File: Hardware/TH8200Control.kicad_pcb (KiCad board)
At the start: 2 copper layers, 113 x 49 mm, 41 parts, among them J1 Mains, J2 Heater Relay, J3 Motor, Q1 BC817, Q2 SFH 300, Q3 BC817, Q4 BC817, T1 BV EI 306 3601, U1 CNY17-3, U2 CNY17-3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

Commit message: Add OSHW logo and GitHub link to PCB
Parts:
- added REF***: OSHW-Symbol_6.7x6mm_SilkScreen, Symbols:OSHW-Symbol_6.7x6mm_SilkScreen, B.Cu at (89.0, 54.5)
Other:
- board text added: "github.com/Mezgrman/TH8200Control"

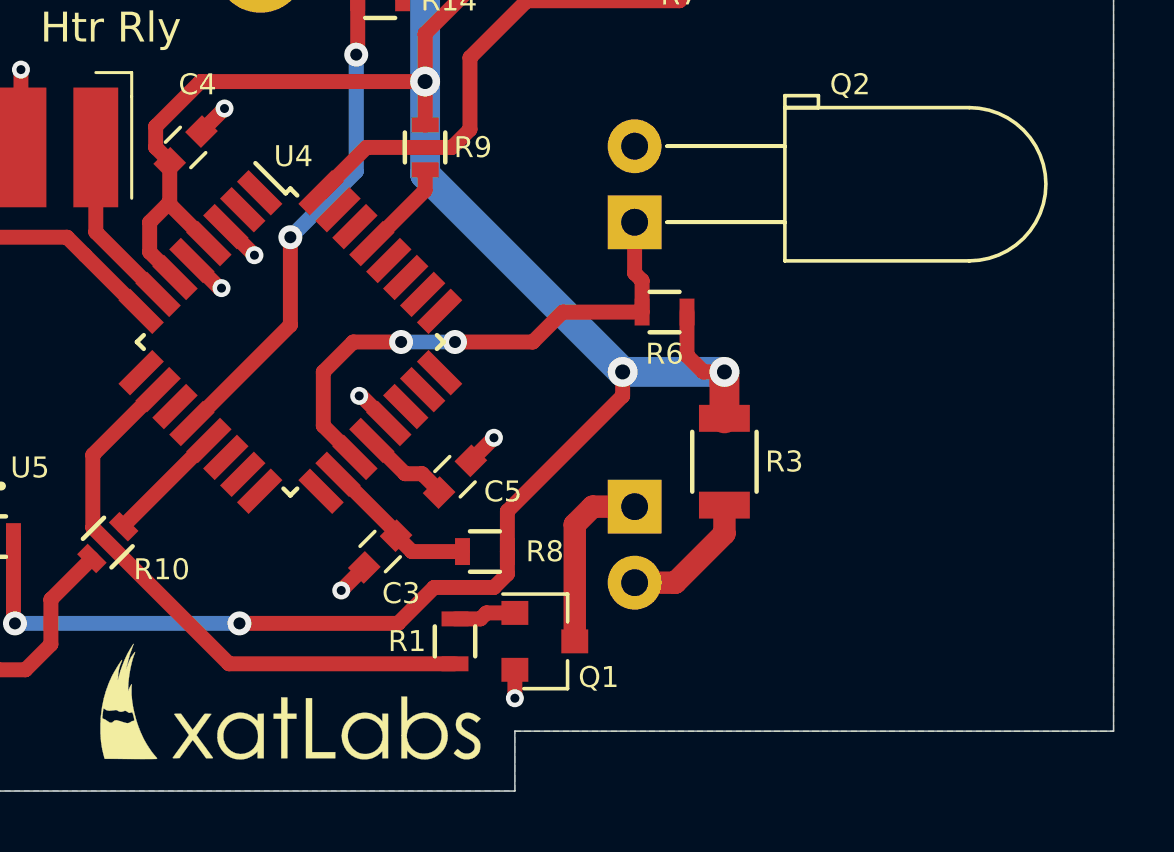
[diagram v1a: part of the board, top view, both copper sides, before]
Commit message: Add ISP header
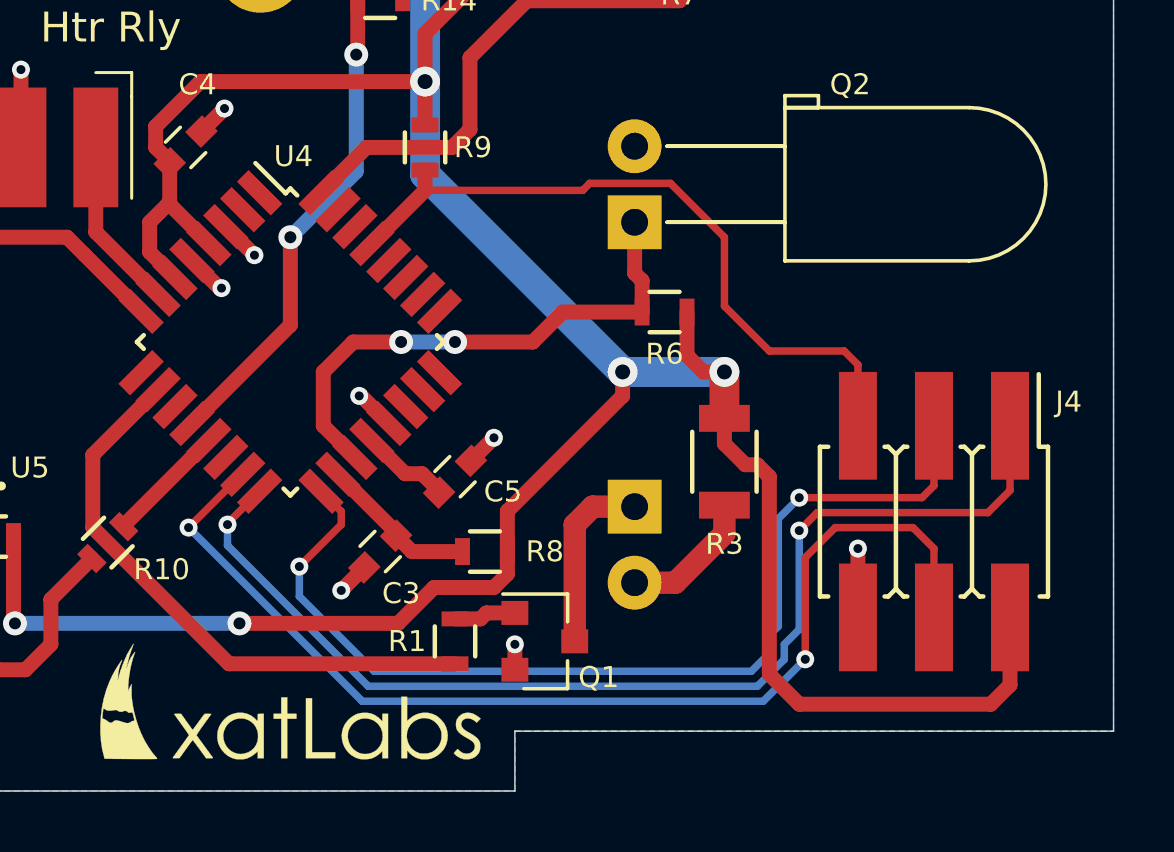
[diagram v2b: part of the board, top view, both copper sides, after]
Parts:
- added J4: ISP, Pin_Headers:Pin_Header_Straight_SMT_02x03, F.Cu at (161.0, 88.0)
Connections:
- net Net-(R9-Pad1) renamed ISP_RESET
- U4 pad 15: Net-(U4-Pad15) -> ISP_COPI
- U4 pad 16: Net-(U4-Pad16) -> ISP_CIPO
- U4 pad 17: Net-(U4-Pad17) -> ISP_SCK
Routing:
- net ISP_CIPO: track 0.00 -> 37.4 mm, vias 0 -> 2
- net ISP_COPI: track 0.00 -> 36.8 mm, vias 0 -> 2
- net ISP_SCK: track 0.00 -> 33.6 mm, vias 0 -> 2
- net ISP_RESET: track 3.20 -> 23.7 mm
- net +5V: track 95.3 -> 115.7 mm
- net GND: track 31.1 -> 33.3 mm, vias 29 -> 30
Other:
- board text added: "Control board for Siemens TH8200 hand dryer v1.0 / 22.07.2020 Julian Metzler xatlabs.com"
- board text removed: "Control board for Siemens TH8200 hand dryer v1.0 / 20.07.2020 Julian Metzler xatlabs.com"

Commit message: Fix polarity of C1
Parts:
- turned C1 to 90 degrees
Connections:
- C1 pad 1: GND -> +12V
- C1 pad 2: +12V -> GND
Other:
- board text added: "Control board for Siemens TH8200 hand dryer v1.1 / 29.07.2020 Julian Metzler xatlabs.com"
- board text removed: "Control board for Siemens TH8200 hand dryer v1.0 / 22.07.2020 Julian Metzler xatlabs.com"
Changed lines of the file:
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@@
   (title_block
     (title "Control board for Siemens TH8200 hand dryer")
-    (date 2020-07-22)
-    (rev 1.0)
+    (date 2020-07-29)
+    (rev 1.1)
     (company xatLabs)
     (comment 1 "Julian Metzler")
@@
   )
   (module Capacitors_SMD:CP_Elec_6.3x7.7 (layer F.Cu)
-    (at 121 54.5 270)
+    (at 121 54.5 90)
     (descr "SMT capacitor, aluminium electrolytic, 6.3x7.7")
     (attr smd)
-    (fp_text reference C1 (at 4.1 2.4) (layer F.SilkS)
-      (effects (font (size 0.7 0.7) (thickness 0.1)))
-    )
-    (fp_text value 100µ/35V/E (at 0 -4.4323 270) (layer F.Fab)
+    (fp_text reference C1 (at 4.1 2.4 -180) (layer F.SilkS)
+      (effects (font (size 0.7 0.7) (thickness 0.1)))
+    )
+    (fp_text value 100µ/35V/E (at 0 -4.4323 90) (layer F.Fab)
       (effects (font (size 1 1) (thickness 0.15)))
     )
@@
     (fp_line (start -2.4765 -3.1496) (end -3.1496 -2.4765) (layer F.Fab) (width 0.1))
     (fp_line (start 3.1496 -3.1496) (end -2.4765 -3.1496) (layer F.Fab) (width 0.1))
-    (fp_text user + (at -1.7272 -0.0762 270) (layer F.Fab)
+    (fp_text user + (at -1.7272 -0.0762 90) (layer F.Fab)
       (effects (font (size 1 1) (thickness 0.15)))
     )
@@
     (fp_line (start 3.302 -3.302) (end 3.302 -1.1176) (layer F.SilkS) (width 0.12))
     (fp_line (start -3.302 -2.54) (end -3.302 -1.1176) (layer F.SilkS) (width 0.12))
-    (fp_text user + (at -4.2799 2.9083 270) (layer F.SilkS)
+    (fp_text user + (at -4.2799 2.9083 90) (layer F.SilkS)
       (effects (font (size 1 1) (thickness 0.15)))
     )
@@
     (fp_line (start -3.302 -2.54) (end -2.54 -3.302) (layer F.SilkS) (width 0.12))
     (fp_line (start -2.54 -3.302) (end 3.302 -3.302) (layer F.SilkS) (width 0.12))
-    (pad 1 smd rect (at -2.7 0 90) (size 3.5 1.6) (layers F.Cu F.Paste F.Mask)
+    (pad 1 smd rect (at -2.7 0 270) (size 3.5 1.6) (layers F.Cu F.Paste F.Mask)
+      (net 2 +12V))
+    (pad 2 smd rect (at 2.7 0 270) (size 3.5 1.6) (layers F.Cu F.Paste F.Mask)
       (net 1 GND))
-    (pad 2 smd rect (at 2.7 0 90) (size 3.5 1.6) (layers F.Cu F.Paste F.Mask)
-      (net 2 +12V))
     (model Capacitors_SMD.3dshapes/CP_Elec_6.3x7.7.wrl
       (at (xyz 0 0 0))
@@
     (effects (font (size 1 1) (thickness 0.15)) (justify mirror))
   )
-  (gr_text "Control board for\nSiemens TH8200 hand dryer\nv1.0 / 22.07.2020\nJulian Metzler\nxatlabs.com" (at 153 62.5) (layer B.SilkS)
+  (gr_text "Control board for\nSiemens TH8200 hand dryer\nv1.1 / 29.07.2020\nJulian Metzler\nxatlabs.com" (at 153 62.5) (layer B.SilkS)
     (effects (font (size 1.2 1.2) (thickness 0.2)) (justify mirror))
   )
